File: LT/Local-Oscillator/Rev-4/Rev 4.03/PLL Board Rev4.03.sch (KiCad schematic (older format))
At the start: 69 parts, among them J1 Conn_01x02_Male, J13 Conn_01x02_Male, J14 Conn_01x02_Male, J15 Conn_01x02_Male, J16 Conn_01x02_Male, J17 Conn_01x02_Male, J18 Conn_Coaxial, J2 Conn_Coaxial, J20 Conn_01x02_Male, J3 Conn_Coaxial, J4 Conn_01x04_Male, J5 Conn_01x02_Male, J7 Conn_01x02_Male, J8 Conn_01x02_Male, Q1 2N5486 JFET, Q2 2N5486 JFET, U1 LMX231X, U2 L7808

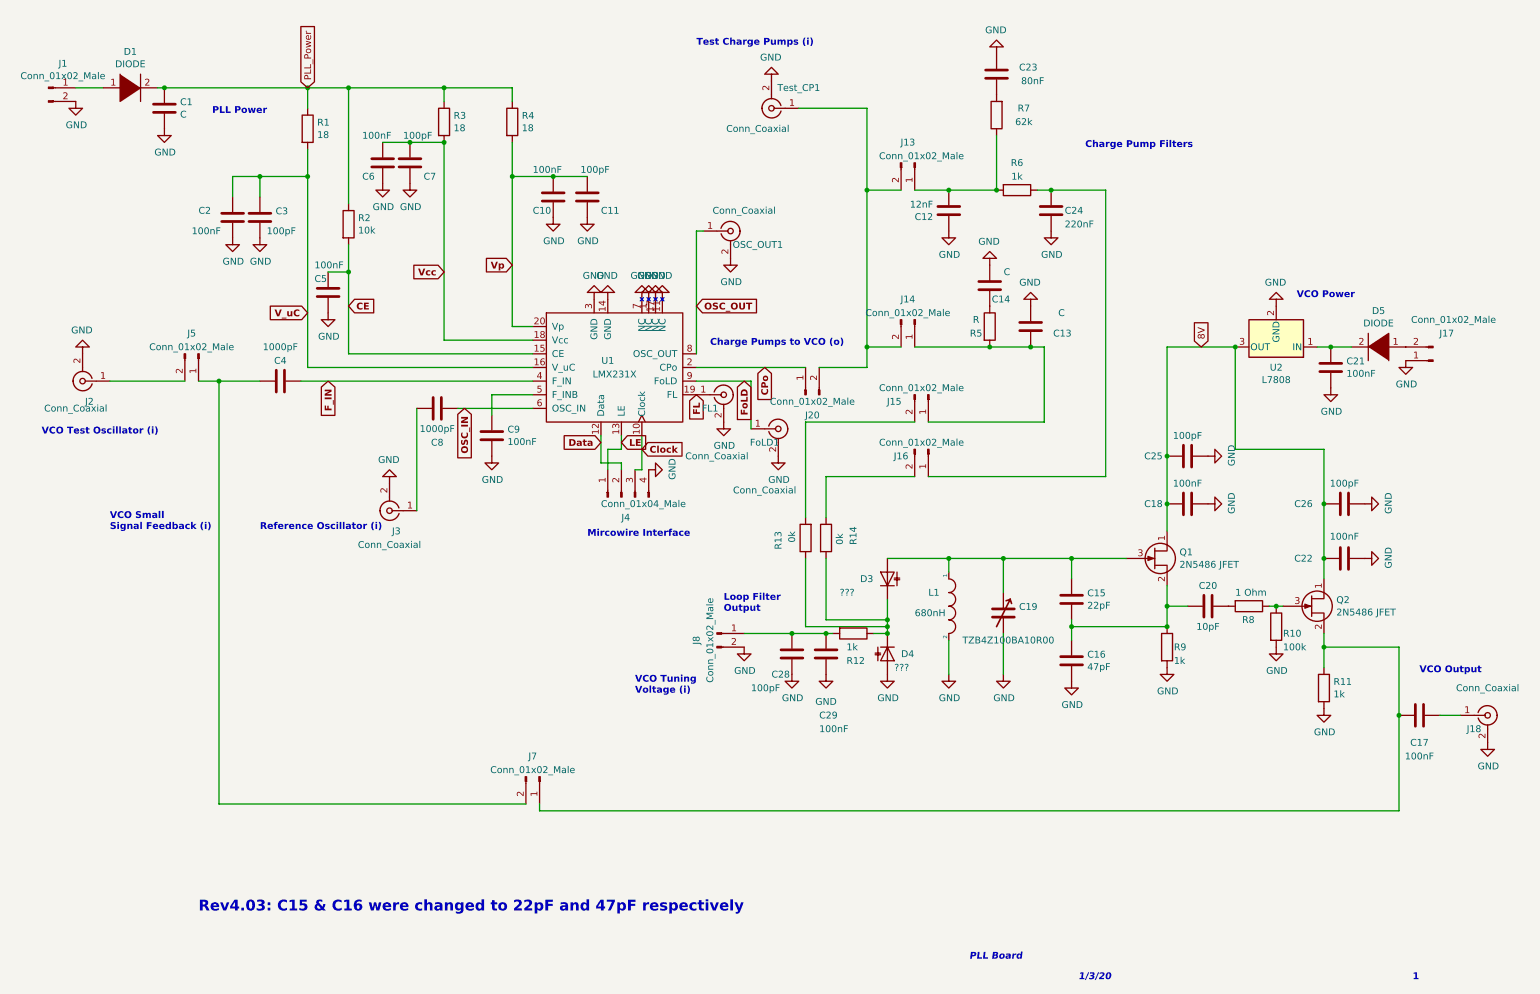
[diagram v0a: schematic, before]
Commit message: Finished PLL Revisions on KiCad
The KiCad files for the PLL have been uploaded to github and the integration to the "Real Resistor" symbol has begun
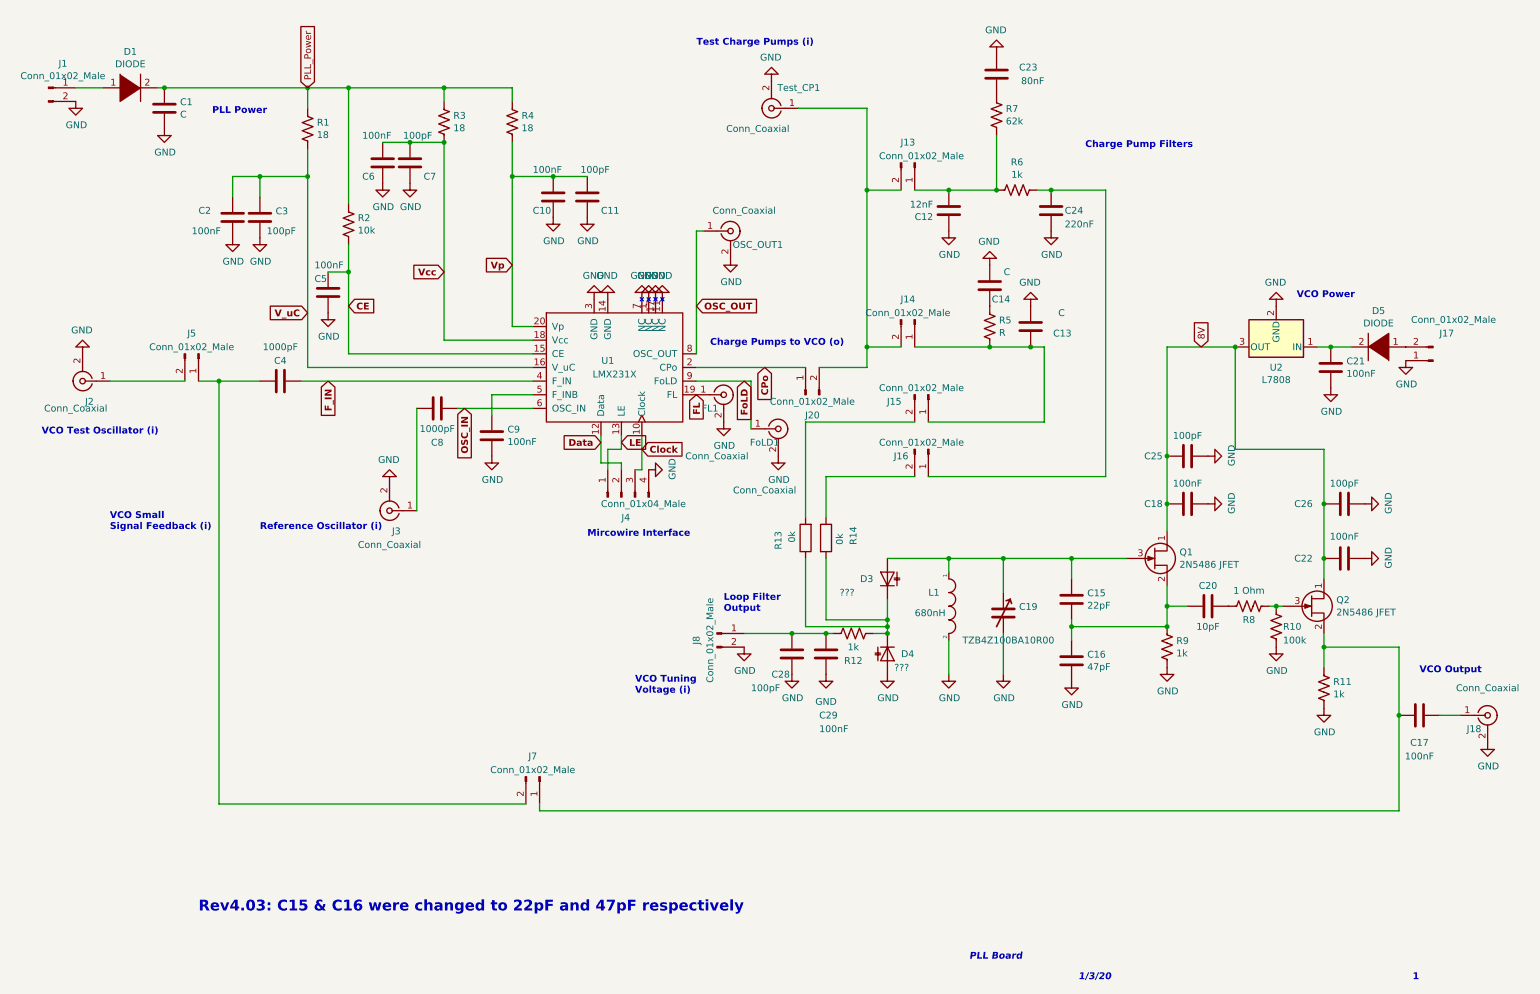
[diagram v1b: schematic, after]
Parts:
- removed R1, R3, R4: 18, Resistor_SMD:R_0805_2012Metric_Pad1.15x1.40mm_HandSolder, symbol PLL-Board-Rev4.03-rescue:R-Device-Complete-PLL-Board-Rev4-rescue-PLL-Board-Rev4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
- removed R10: 100k, Resistor_SMD:R_0805_2012Metric_Pad1.15x1.40mm_HandSolder, symbol PLL-Board-Rev4.03-rescue:R-Device-Complete-PLL-Board-Rev4-rescue-PLL-Board-Rev4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
- removed R11, R12, R6, R9: 1k, Resistor_SMD:R_0805_2012Metric_Pad1.15x1.40mm_HandSolder, symbol PLL-Board-Rev4.03-rescue:R-Device-Complete-PLL-Board-Rev4-rescue-PLL-Board-Rev4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
- removed R2: 10k, Resistor_SMD:R_0805_2012Metric_Pad1.15x1.40mm_HandSolder, symbol PLL-Board-Rev4.03-rescue:R-Device-Complete-PLL-Board-Rev4-rescue-PLL-Board-Rev4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
- removed R5: R, Resistor_SMD:R_0805_2012Metric_Pad1.15x1.40mm_HandSolder, symbol PLL-Board-Rev4.03-rescue:R-Device-Complete-PLL-Board-Rev4-rescue-PLL-Board-Rev4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
- removed R7: 62k, Resistor_SMD:R_0805_2012Metric_Pad1.15x1.40mm_HandSolder, symbol PLL-Board-Rev4.03-rescue:R-Device-Complete-PLL-Board-Rev4-rescue-PLL-Board-Rev4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
- removed R8: 1 Ohm, Resistor_SMD:R_0805_2012Metric_Pad1.15x1.40mm_HandSolder, symbol PLL-Board-Rev4.03-rescue:R-Device-Complete-PLL-Board-Rev4-rescue-PLL-Board-Rev4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
- added R1, R3, R4: 18, Resistor_SMD:R_0805_2012Metric_Pad1.15x1.40mm_HandSolder, symbol Device:R
- added R10: 100k, Resistor_SMD:R_0805_2012Metric_Pad1.15x1.40mm_HandSolder, symbol Device:R
- added R11, R12, R6, R9: 1k, Resistor_SMD:R_0805_2012Metric_Pad1.15x1.40mm_HandSolder, symbol Device:R
- added R2: 10k, Resistor_SMD:R_0805_2012Metric_Pad1.15x1.40mm_HandSolder, symbol Device:R
- added R5: R, Resistor_SMD:R_0805_2012Metric_Pad1.15x1.40mm_HandSolder, symbol Device:R
- added R7: 62k, Resistor_SMD:R_0805_2012Metric_Pad1.15x1.40mm_HandSolder, symbol Device:R
- added R8: 1 Ohm, Resistor_SMD:R_0805_2012Metric_Pad1.15x1.40mm_HandSolder, symbol Device:R
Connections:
- net CE: now also R2.2
- net GND: now also R10.2, R11.2, R9.2
- net PLL_Power: now also R1.1, R2.1, R3.1, R4.1
- net V_uC: now also R1.2
- net Vcc: now also R3.2
- net Vp: now also R4.2
- net at C15.1, C16.2, C20.1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: now also R9.1
- net at D3.1 (K), D4.1 (K), R13.1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: now also R12.1
- net at C20.2: now also R8.2
- net at Q2.3 (G): now also R10.1, R8.1
- net at C17.1, J7.1 (Pin_1), Q2.2 (S): now also R11.1
- net at C13.1, J14.1 (Pin_1), J15.1 (Pin_1): now also R5.2
- net at C12.2, J13.1 (Pin_1): now also R6.2, R7.2
- net at C24.1, J16.1 (Pin_1): now also R6.1
- net at C28.2, C29.2, J8.1 (Pin_1): now also R12.2
- net at C14.1: now also R5.1
- net at C23.1: now also R7.1

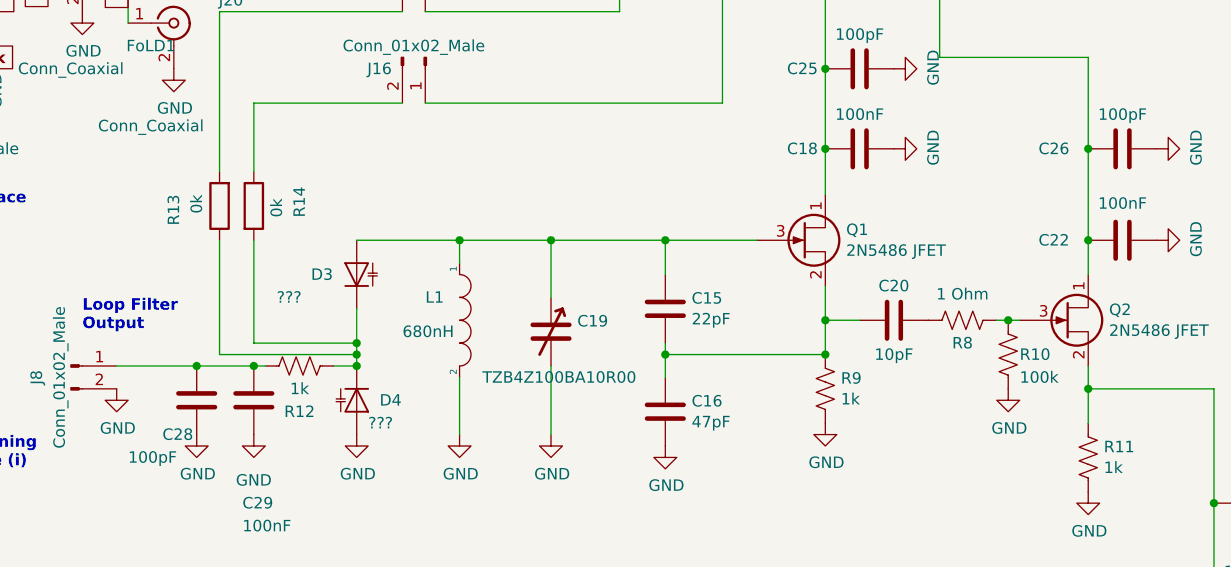
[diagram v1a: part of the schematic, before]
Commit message: Changed Resistor Symbols
Fixed the resistor symbols from PLL Rev 4.1-4.3
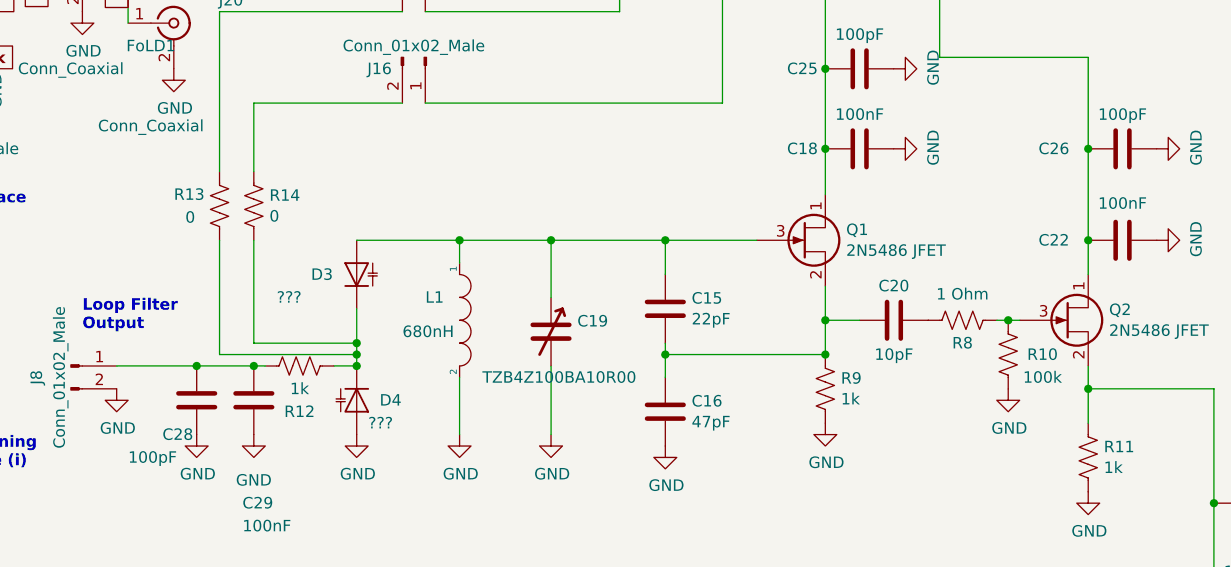
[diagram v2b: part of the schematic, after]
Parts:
- removed R1, R3, R4: 18, Resistor_SMD:R_0805_2012Metric_Pad1.15x1.40mm_HandSolder, symbol Device:R
- removed R10: 100k, Resistor_SMD:R_0805_2012Metric_Pad1.15x1.40mm_HandSolder, symbol Device:R
- removed R11, R12, R6, R9: 1k, Resistor_SMD:R_0805_2012Metric_Pad1.15x1.40mm_HandSolder, symbol Device:R
- removed R13, R14: 0k, Resistor_SMD:R_0805_2012Metric_Pad1.15x1.40mm_HandSolder, symbol PLL-Board-Rev4.03-rescue:R-Device-Complete-PLL-Board-Rev4-rescue-PLL-Board-Rev4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
- removed R2: 10k, Resistor_SMD:R_0805_2012Metric_Pad1.15x1.40mm_HandSolder, symbol Device:R
- removed R5: R, Resistor_SMD:R_0805_2012Metric_Pad1.15x1.40mm_HandSolder, symbol Device:R
- removed R7: 62k, Resistor_SMD:R_0805_2012Metric_Pad1.15x1.40mm_HandSolder, symbol Device:R
- removed R8: 1 Ohm, Resistor_SMD:R_0805_2012Metric_Pad1.15x1.40mm_HandSolder, symbol Device:R
- added R1, R3, R4: 18, Resistor_SMD:R_0805_2012Metric_Pad1.15x1.40mm_HandSolder, symbol Device:R_US
- added R10: 100k, Resistor_SMD:R_0805_2012Metric_Pad1.15x1.40mm_HandSolder, symbol Device:R_US
- added R11, R12, R6, R9: 1k, Resistor_SMD:R_0805_2012Metric_Pad1.15x1.40mm_HandSolder, symbol Device:R_US
- added R13, R14: 0, Resistor_SMD:R_0805_2012Metric_Pad1.15x1.40mm_HandSolder, symbol Device:R_US
- added R2: 10k, Resistor_SMD:R_0805_2012Metric_Pad1.15x1.40mm_HandSolder, symbol Device:R_US
- added R5: R, Resistor_SMD:R_0805_2012Metric_Pad1.15x1.40mm_HandSolder, symbol Device:R_US
- added R7: 62k, Resistor_SMD:R_0805_2012Metric_Pad1.15x1.40mm_HandSolder, symbol Device:R_US
- added R8: 1 Ohm, Resistor_SMD:R_0805_2012Metric_Pad1.15x1.40mm_HandSolder, symbol Device:R_US
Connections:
- net CE: now also R2.2
- net GND: now also R10.1, R11.2, R9.2
- net PLL_Power: now also R1.1, R2.1, R3.1, R4.1
- net V_uC: now also R1.2
- net Vcc: now also R3.2
- net Vp: now also R4.2
- net at C15.1, C16.2, C20.1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: now also R9.1
- net at D3.1 (K), D4.1 (K): now also R12.1, R13.2, R14.2
- net at C20.2: now also R8.2
- net at C13.1, J14.1 (Pin_1), J15.1 (Pin_1): now also R5.2
- net at C12.2, J13.1 (Pin_1): now also R6.2, R7.2
- net at C17.1, J7.1 (Pin_1), Q2.2 (S): now also R11.1
- net at Q2.3 (G): now also R10.2, R8.1
- net at J15.2 (Pin_2): now also R13.1
- net at C28.2, C29.2, J8.1 (Pin_1): now also R12.2
- net at C14.1: now also R5.1
- net at C24.1, J16.1 (Pin_1): now also R6.1
- net at J16.2 (Pin_2): now also R14.1
- net at C23.1: now also R7.1
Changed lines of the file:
@@
 Wire Wire Line
 	8800 4900 8950 4900
-$Comp
-L PLL-Board-Rev4.03-rescue:R-Device-Complete-PLL-Board-Rev4-rescue-PLL-Board-Rev4.01-rescue-PLL-Board-Rev4.02-rescue R13
-U 1 1 5CBB0D39
-P 6150 4400
-F 0 "R13" V 6350 4350 50  0000 L CNN
-F 1 "0k" V 6250 4350 50  0000 L CNN
-F 2 "Resistor_SMD:R_0805_2012Metric_Pad1.15x1.40mm_HandSolder" V 6080 4400 50  0001 C CNN
-F 3 "~" H 6150 4400 50  0001 C CNN
-	1    6150 4400
-	-1   0    0    1
-$EndComp
-$Comp
-L PLL-Board-Rev4.03-rescue:R-Device-Complete-PLL-Board-Rev4-rescue-PLL-Board-Rev4.01-rescue-PLL-Board-Rev4.02-rescue R14
-U 1 1 5CBBAAF0
-P 6300 4400
-F 0 "R14" V 6500 4350 50  0000 L CNN
-F 1 "0k" V 6400 4350 50  0000 L CNN
-F 2 "Resistor_SMD:R_0805_2012Metric_Pad1.15x1.40mm_HandSolder" V 6230 4400 50  0001 C CNN
-F 3 "~" H 6300 4400 50  0001 C CNN
-	1    6300 4400
-	1    0    0    -1
-$EndComp
 Wire Wire Line
 	6300 3950 6300 4250
@@
 Text Notes 1700 7150 0    79   ~ 16
 Rev4.03: C15 & C16 were changed to 22pF and 47pF respectively
-$Comp
-L Device:R R1
-U 1 1 5E5B44C7
+Wire Wire Line
+	7550 1450 7550 1850
+$Comp
+L Device:R_US R1
+U 1 1 5E5B7761
 P 2500 1400
 F 0 "R1" H 2568 1446 50  0000 L CNN
@@
 $EndComp
 $Comp
-L Device:R R3
-U 1 1 5E5B9B47
+L Device:R_US R3
+U 1 1 5E5BCAEE
 P 3500 1350
 F 0 "R3" H 3568 1396 50  0000 L CNN
@@
 	1    0    0    -1
 $EndComp
-$Comp
-L Device:R R4
-U 1 1 5E5BA584
+Connection ~ 3500 1500
+$Comp
+L Device:R_US R2
+U 1 1 5E5C1CE4
+P 2800 2100
+F 0 "R2" H 2868 2146 50  0000 L CNN
+F 1 "10k" H 2868 2055 50  0000 L CNN
+F 2 "Resistor_SMD:R_0805_2012Metric_Pad1.15x1.40mm_HandSolder" V 2840 2090 50  0001 C CNN
+F 3 "~" H 2800 2100 50  0001 C CNN
+	1    2800 2100
+	1    0    0    -1
+$EndComp
+$Comp
+L Device:R_US R4
+U 1 1 5E5C7B55
 P 4000 1350
 F 0 "R4" H 4068 1396 50  0000 L CNN
@@
 $EndComp
 $Comp
-L Device:R R2
-U 1 1 5E5BAE2B
-P 2800 2100
-F 0 "R2" H 2868 2146 50  0000 L CNN
-F 1 "10k" H 2868 2055 50  0000 L CNN
-F 2 "Resistor_SMD:R_0805_2012Metric_Pad1.15x1.40mm_HandSolder" V 2840 2090 50  0001 C CNN
-F 3 "~" H 2800 2100 50  0001 C CNN
-	1    2800 2100
-	1    0    0    -1
-$EndComp
-$Comp
-L Device:R R12
-U 1 1 5E5BB6EA
+L Device:R_US R13
+U 1 1 5E5CC974
+P 6150 4400
+F 0 "R13" H 5950 4450 50  0000 L CNN
+F 1 "0" H 6000 4350 50  0000 L CNN
+F 2 "Resistor_SMD:R_0805_2012Metric_Pad1.15x1.40mm_HandSolder" V 6190 4390 50  0001 C CNN
+F 3 "~" H 6150 4400 50  0001 C CNN
+	1    6150 4400
+	1    0    0    -1
+$EndComp
+$Comp
+L Device:R_US R14
+U 1 1 5E5CD5D3
+P 6300 4400
+F 0 "R14" H 6368 4446 50  0000 L CNN
+F 1 "0" H 6368 4355 50  0000 L CNN
+F 2 "Resistor_SMD:R_0805_2012Metric_Pad1.15x1.40mm_HandSolder" V 6340 4390 50  0001 C CNN
+F 3 "~" H 6300 4400 50  0001 C CNN
+	1    6300 4400
+	1    0    0    -1
+$EndComp
+$Comp
+L Device:R_US R12
+U 1 1 5E5D7D5A
 P 6500 5100
 F 0 "R12" V 6700 5100 50  0000 C CNN
@@
 $EndComp
 $Comp
-L Device:R R9
-U 1 1 5E5BC174
+L Device:R_US R9
+U 1 1 5E5DE536
 P 8800 5200
 F 0 "R9" H 8868 5246 50  0000 L CNN
@@
 	1    0    0    -1
 $EndComp
-$Comp
-L Device:R R11
-U 1 1 5E5BCA63
+Connection ~ 8800 5050
+$Comp
+L Device:R_US R8
+U 1 1 5E5E44F2
+P 9400 4900
+F 0 "R8" V 9500 4900 50  0000 C CNN
+F 1 "1 Ohm" V 9286 4900 50  0000 C CNN
+F 2 "Resistor_SMD:R_0805_2012Metric_Pad1.15x1.40mm_HandSolder" V 9440 4890 50  0001 C CNN
+F 3 "~" H 9400 4900 50  0001 C CNN
+	1    9400 4900
+	0    1    1    0
+$EndComp
+$Comp
+L Device:R_US R10
+U 1 1 5E5EA354
+P 9600 5050
+F 0 "R10" H 9450 5050 50  0000 C CNN
+F 1 "100k" H 9450 5150 50  0000 C CNN
+F 2 "Resistor_SMD:R_0805_2012Metric_Pad1.15x1.40mm_HandSolder" V 9640 5040 50  0001 C CNN
+F 3 "~" H 9600 5050 50  0001 C CNN
+	1    9600 5050
+	-1   0    0    1
+$EndComp
+Wire Wire Line
+	9550 4900 9600 4900
+Connection ~ 9600 4900
+Wire Wire Line
+	9600 4900 9650 4900
+$Comp
+L Device:R_US R11
+U 1 1 5E5EFA99
 P 9950 5500
 F 0 "R11" H 10018 5546 50  0000 L CNN
@@
 $EndComp
 $Comp
-L Device:R R10
-U 1 1 5E5BD36A
-P 9600 5050
-F 0 "R10" H 9650 5050 50  0000 L CNN
-F 1 "100k" H 9650 4950 50  0000 L CNN
-F 2 "Resistor_SMD:R_0805_2012Metric_Pad1.15x1.40mm_HandSolder" V 9640 5040 50  0001 C CNN
-F 3 "~" H 9600 5050 50  0001 C CNN
-	1    9600 5050
-	1    0    0    -1
-$EndComp
-$Comp
-L Device:R R8
-U 1 1 5E5BDC89
-P 9400 4900
-F 0 "R8" V 9500 4900 50  0000 C CNN
-F 1 "1 Ohm" V 9286 4900 50  0000 C CNN
-F 2 "Resistor_SMD:R_0805_2012Metric_Pad1.15x1.40mm_HandSolder" V 9440 4890 50  0001 C CNN
-F 3 "~" H 9400 4900 50  0001 C CNN
-	1    9400 4900
-	0    1    1    0
-$EndComp
-$Comp
-L Device:R R5
-U 1 1 5E5BE5C0
+L Device:R_US R5
+U 1 1 5E5F4B63
 P 7500 2850
 F 0 "R5" H 7568 2896 50  0000 L CNN
@@
 	1    0    0    -1
 $EndComp
-$Comp
-L Device:R R6
-U 1 1 5E5BEF0F
+Wire Wire Line
+	6950 3000 7500 3000
+Connection ~ 7500 3000
+Wire Wire Line
+	7500 3000 7800 3000
+$Comp
+L Device:R_US R6
+U 1 1 5E5FA494
 P 7700 1850
 F 0 "R6" V 7495 1850 50  0000 C CNN
@@
 	0    1    1    0
 $EndComp
-$Comp
-L Device:R R7
-U 1 1 5E5BF876
+Connection ~ 7550 1850
+$Comp
+L Device:R_US R7
+U 1 1 5E600879
 P 7550 1300
 F 0 "R7" H 7618 1346 50  0000 L CNN
@@
 	1    0    0    -1
 $EndComp
-Connection ~ 3500 1500
-Connection ~ 8800 5050
-Wire Wire Line
-	9550 4900 9600 4900
-Connection ~ 9600 4900
-Wire Wire Line
-	9600 4900 9650 4900
-Wire Wire Line
-	6950 3000 7500 3000
-Connection ~ 7500 3000
-Wire Wire Line
-	7500 3000 7800 3000
-Wire Wire Line
-	7550 1450 7550 1850
-Connection ~ 7550 1850
 $EndSCHEMATC
